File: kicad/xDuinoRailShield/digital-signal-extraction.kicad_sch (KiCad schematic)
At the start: 8 parts, among them U2 6N137, U3 EL817

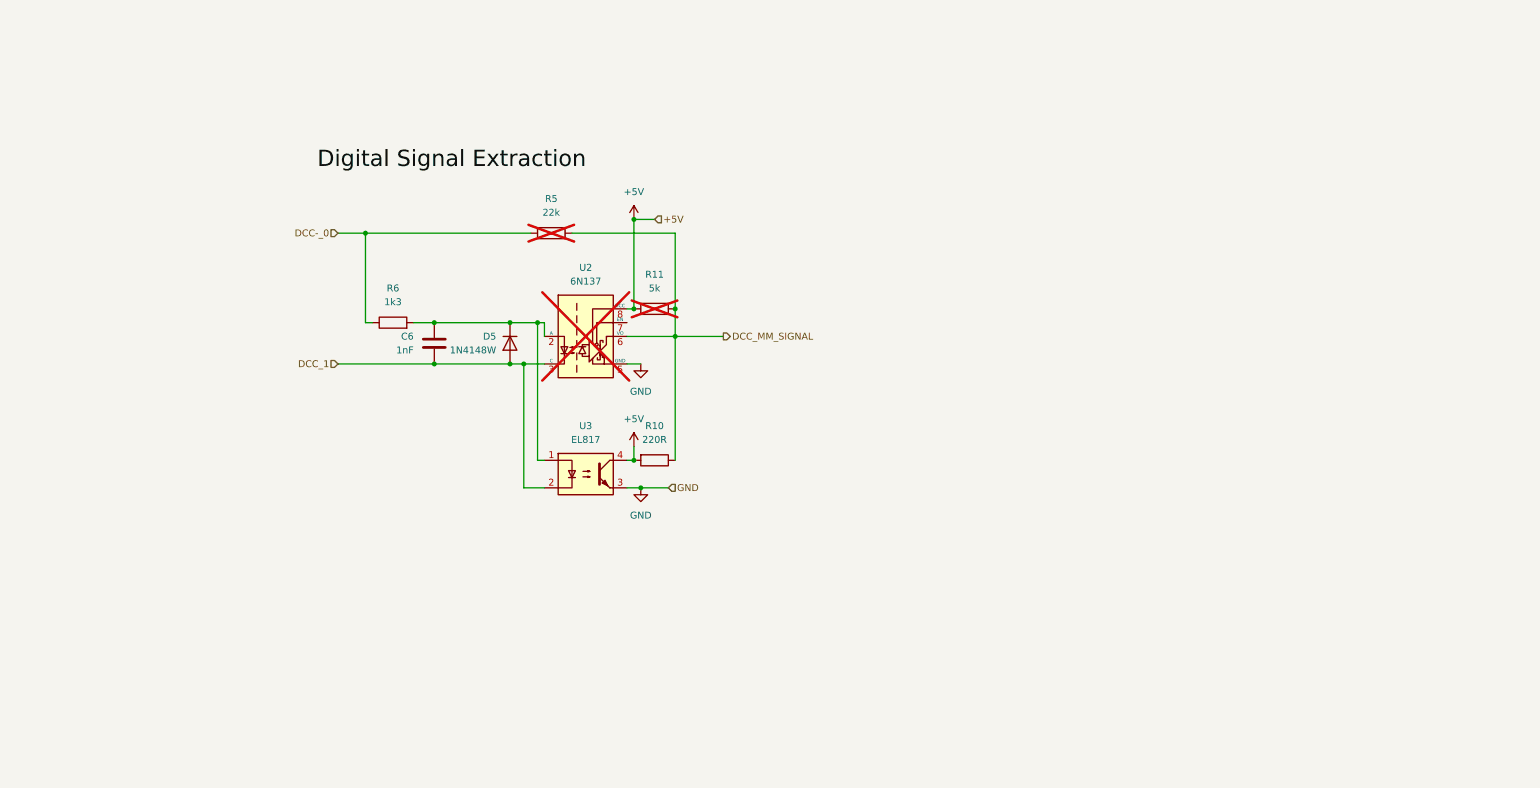
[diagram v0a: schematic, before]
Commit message: Add more extractor
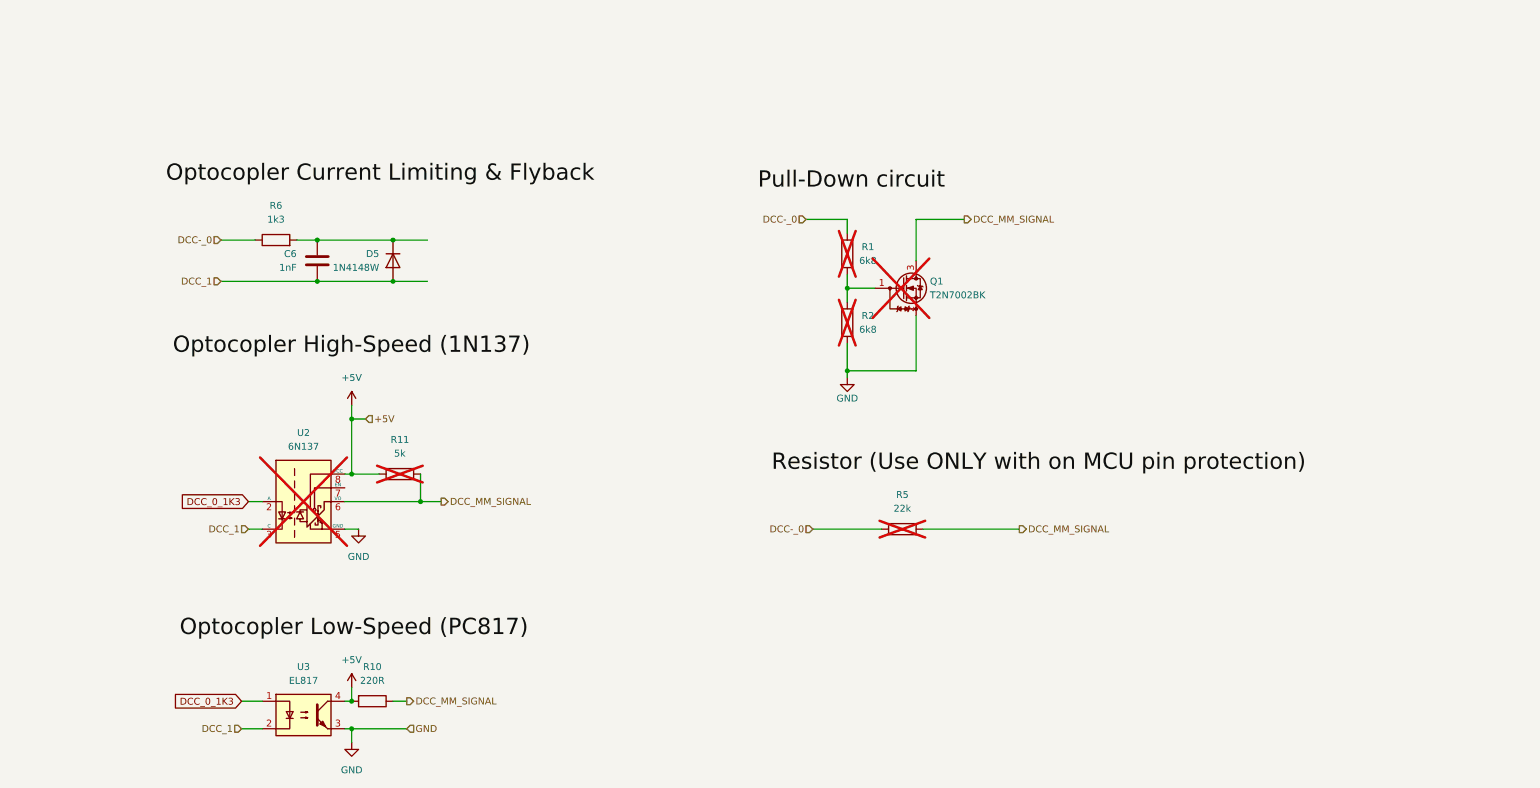
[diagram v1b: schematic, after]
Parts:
- added Q1: T2N7002BK, Package_TO_SOT_SMD:SOT-23, symbol RP2040-Decoder_Additional_Symbols:T2N7002BK
- added R1, R2: 6k8, RP2040-Decoder_Additional_Footprints:R_0603_1608Metric, symbol Device:R
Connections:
- net DCC_MM_SIGNAL: now also Q1.3 (D)
- net DCC­_0: now also R1.2
- net GND: now also Q1.2 (S), R2.1
- net at C6.1, D5.1 (K), R6.2: no longer U2.2 (A), U3.1
- new net: Q1.1 (G), R1.1, R2.2
- new net DCC_0_1K3: U2.2 (A), U3.1
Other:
- moved on the sheet: C6, D5, R6

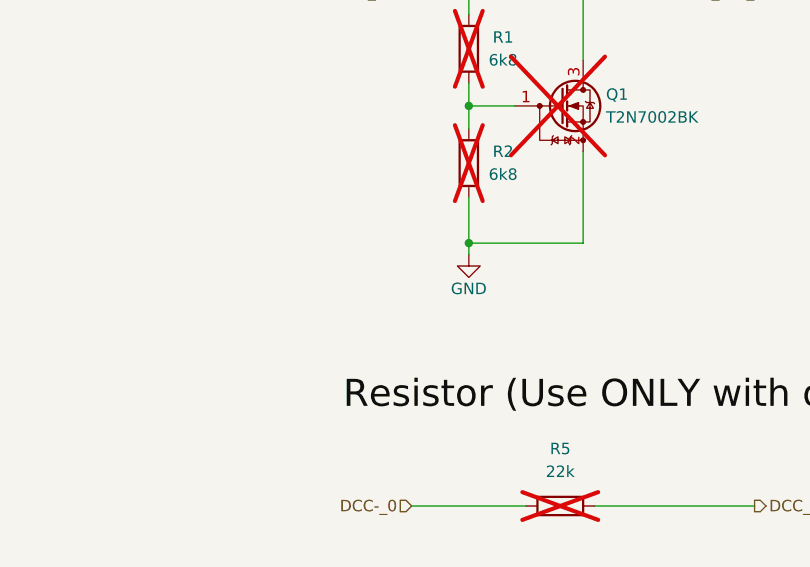
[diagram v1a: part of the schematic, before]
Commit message: More options, more Partnumbers
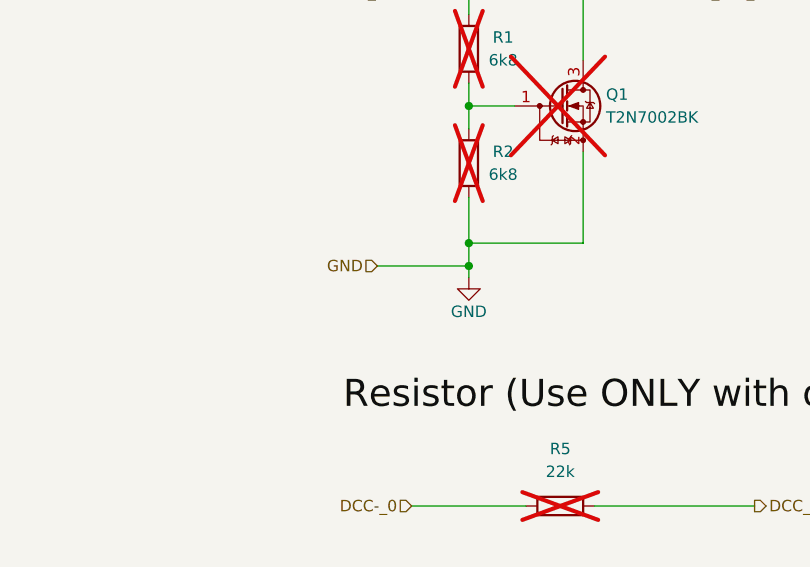
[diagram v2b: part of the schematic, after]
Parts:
- Q1: LCSC (none) -> C8545
- R1, R2: footprint RP2040-Decoder_Additional_Footprints:R_0603_1608Metric -> Resistor_SMD:R_0805_2012Metric_Pad1.20x1.40mm_HandSolder; LCSC (none) -> C17772
- R5: now left out of the parts list
- U2: LCSC (none) -> C16496; now left out of the parts list
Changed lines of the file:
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@@
   (junction (at 74.93 148.59) (diameter 0) (color 0 0 0 0)
   )
+  (junction (at 166.37 90.17) (diameter 0) (color 0 0 0 0)
+  )
   (junction (at 87.63 111.76) (diameter 0) (color 0 0 0 0)
   )
@@
     (stroke (width 0) (type default))
   )
+  (wire (pts (xy 156.21 90.17) (xy 166.37 90.17))
+    (stroke (width 0) (type default))
+  )
   (wire (pts (xy 179.07 77.47) (xy 179.07 87.63))
     (stroke (width 0) (type default))
@@
     (stroke (width 0) (type default))
   )
+  (wire (pts (xy 166.37 90.17) (xy 166.37 87.63))
+    (stroke (width 0) (type default))
+  )
   (wire (pts (xy 166.37 72.39) (xy 171.45 72.39))
     (stroke (width 0) (type default))
@@
     (stroke (width 0) (type default))
   )
-  (wire (pts (xy 166.37 88.9) (xy 166.37 87.63))
+  (wire (pts (xy 166.37 91.44) (xy 166.37 90.17))
     (stroke (width 0) (type default))
   )
@@
     (effects (font (size 1.27 1.27)) (justify left))
   )
+  (hierarchical_label "GND" (shape input) (at 156.21 90.17 180) (fields_autoplaced)
+    (effects (font (size 1.27 1.27)) (justify right))
+  )
   (hierarchical_label "DCC_1" (shape input) (at 54.61 153.67 180) (fields_autoplaced)
     (effects (font (size 1.27 1.27)) (justify right))
@@
   )
   (symbol (lib_id "Device:R") (at 166.37 66.04 180) (unit 1)
-    (in_bom no) (on_board no) (dnp yes)
+    (in_bom no) (on_board yes) (dnp yes)
     (property "Reference" "R1" (at 170.18 64.77 0)
       (effects (font (size 1.27 1.27)))
@@
       (effects (font (size 1.27 1.27)))
     )
-    (property "Footprint" "RP2040-Decoder_Additional_Footprints:R_0603_1608Metric" (at 168.148 66.04 90)
+    (property "Footprint" "Resistor_SMD:R_0805_2012Metric_Pad1.20x1.40mm_HandSolder" (at 168.148 66.04 90)
       (effects (font (size 1.27 1.27)) hide)
     )
     (property "Datasheet" "~" (at 166.37 66.04 0)
+      (effects (font (size 1.27 1.27)) hide)
+    )
+    (property "LCSC" "C17772" (at 166.37 66.04 0)
       (effects (font (size 1.27 1.27)) hide)
     )
@@
       (project "xDuinoRailShield"
         (path "/e63e39d7-6ac0-4ffd-8aa3-1841a4541b55/b84a333b-f29e-43df-b84d-edef752a64aa"
-          (reference "R11") (unit 1)
+          (reference "R304") (unit 1)
         )
       )
@@
         )
         (path "/e63e39d7-6ac0-4ffd-8aa3-1841a4541b55/b84a333b-f29e-43df-b84d-edef752a64aa"
-          (reference "#PWR06") (unit 1)
+          (reference "#PWR0303") (unit 1)
         )
       )
@@
   )
   (symbol (lib_id "RP2040-Decoder_Additional_Symbols:T2N7002BK") (at 176.53 72.39 0) (unit 1)
-    (in_bom no) (on_board no) (dnp yes)
+    (in_bom no) (on_board yes) (dnp yes)
     (property "Reference" "Q1" (at 181.61 71.12 0)
       (effects (font (size 1.27 1.27)) (justify left))
@@
     )
     (property "Datasheet" "https://datasheet.lcsc.com/lcsc/1810271831_TOSHIBA-T2N7002BK-LM_C146372.pdf" (at 190.5 83.82 0)
+      (effects (font (size 1.27 1.27)) hide)
+    )
+    (property "LCSC" "C8545" (at 176.53 72.39 0)
       (effects (font (size 1.27 1.27)) hide)
     )
@@
       (project "xDuinoRailShield"
         (path "/e63e39d7-6ac0-4ffd-8aa3-1841a4541b55/b84a333b-f29e-43df-b84d-edef752a64aa"
-          (reference "Q5") (unit 1)
+          (reference "Q301") (unit 1)
         )
       )
@@
         )
         (path "/e63e39d7-6ac0-4ffd-8aa3-1841a4541b55/b84a333b-f29e-43df-b84d-edef752a64aa"
-          (reference "D4") (unit 1)
+          (reference "D301") (unit 1)
         )
       )
@@
         )
         (path "/e63e39d7-6ac0-4ffd-8aa3-1841a4541b55/b84a333b-f29e-43df-b84d-edef752a64aa"
-          (reference "#PWR02") (unit 1)
+          (reference "#PWR0301") (unit 1)
         )
       )
@@
         )
         (path "/e63e39d7-6ac0-4ffd-8aa3-1841a4541b55/b84a333b-f29e-43df-b84d-edef752a64aa"
-          (reference "R5") (unit 1)
+          (reference "R303") (unit 1)
         )
       )
@@
         )
         (path "/e63e39d7-6ac0-4ffd-8aa3-1841a4541b55/b84a333b-f29e-43df-b84d-edef752a64aa"
-          (reference "#PWR05") (unit 1)
+          (reference "#PWR0304") (unit 1)
         )
       )
@@
         )
         (path "/e63e39d7-6ac0-4ffd-8aa3-1841a4541b55/b84a333b-f29e-43df-b84d-edef752a64aa"
-          (reference "#PWR04") (unit 1)
-        )
-      )
-    )
-  )
-  (symbol (lib_id "power:GND") (at 166.37 88.9 0) (mirror y) (unit 1)
+          (reference "#PWR0302") (unit 1)
+        )
+      )
+    )
+  )
+  (symbol (lib_id "power:GND") (at 166.37 91.44 0) (mirror y) (unit 1)
     (in_bom yes) (on_board yes) (dnp no)
-    (property "Reference" "#PWR08" (at 166.37 95.25 0)
-      (effects (font (size 1.27 1.27)) hide)
-    )
-    (property "Value" "GND" (at 166.37 92.71 0)
-      (effects (font (size 1.27 1.27)))
-    )
-    (property "Footprint" "" (at 166.37 88.9 0)
-      (effects (font (size 1.27 1.27)) hide)
-    )
-    (property "Datasheet" "" (at 166.37 88.9 0)
+    (property "Reference" "#PWR08" (at 166.37 97.79 0)
+      (effects (font (size 1.27 1.27)) hide)
+    )
+    (property "Value" "GND" (at 166.37 95.25 0)
+      (effects (font (size 1.27 1.27)))
+    )
+    (property "Footprint" "" (at 166.37 91.44 0)
+      (effects (font (size 1.27 1.27)) hide)
+    )
+    (property "Datasheet" "" (at 166.37 91.44 0)
       (effects (font (size 1.27 1.27)) hide)
     )
@@
       (project "xDuinoRailShield"
         (path "/e63e39d7-6ac0-4ffd-8aa3-1841a4541b55/b84a333b-f29e-43df-b84d-edef752a64aa"
-          (reference "#PWR018") (unit 1)
+          (reference "#PWR0305") (unit 1)
         )
       )
@@
         )
         (path "/e63e39d7-6ac0-4ffd-8aa3-1841a4541b55/b84a333b-f29e-43df-b84d-edef752a64aa"
-          (reference "U3") (unit 1)
+          (reference "U302") (unit 1)
         )
       )
@@
         )
         (path "/e63e39d7-6ac0-4ffd-8aa3-1841a4541b55/b84a333b-f29e-43df-b84d-edef752a64aa"
-          (reference "R6") (unit 1)
+          (reference "R302") (unit 1)
         )
       )
@@
         )
         (path "/e63e39d7-6ac0-4ffd-8aa3-1841a4541b55/b84a333b-f29e-43df-b84d-edef752a64aa"
-          (reference "C1") (unit 1)
+          (reference "C301") (unit 1)
         )
       )
@@
   )
   (symbol (lib_id "Device:R") (at 166.37 78.74 180) (unit 1)
-    (in_bom no) (on_board no) (dnp yes)
+    (in_bom no) (on_board yes) (dnp yes)
     (property "Reference" "R2" (at 170.18 77.47 0)
       (effects (font (size 1.27 1.27)))
@@
       (effects (font (size 1.27 1.27)))
     )
-    (property "Footprint" "RP2040-Decoder_Additional_Footprints:R_0603_1608Metric" (at 168.148 78.74 90)
+    (property "Footprint" "Resistor_SMD:R_0805_2012Metric_Pad1.20x1.40mm_HandSolder" (at 168.148 78.74 90)
       (effects (font (size 1.27 1.27)) hide)
     )
     (property "Datasheet" "~" (at 166.37 78.74 0)
+      (effects (font (size 1.27 1.27)) hide)
+    )
+    (property "LCSC" "C17772" (at 166.37 78.74 0)
       (effects (font (size 1.27 1.27)) hide)
     )
@@
       (project "xDuinoRailShield"
         (path "/e63e39d7-6ac0-4ffd-8aa3-1841a4541b55/b84a333b-f29e-43df-b84d-edef752a64aa"
-          (reference "R14") (unit 1)
+          (reference "R305") (unit 1)
         )
       )
@@
   )
   (symbol (lib_id "Device:R") (at 176.53 116.84 90) (unit 1)
-    (in_bom yes) (on_board yes) (dnp yes) (fields_autoplaced)
+    (in_bom no) (on_board yes) (dnp yes) (fields_autoplaced)
     (property "Reference" "R5" (at 176.53 110.49 90)
       (effects (font (size 1.27 1.27)))
@@
         )
         (path "/e63e39d7-6ac0-4ffd-8aa3-1841a4541b55/b84a333b-f29e-43df-b84d-edef752a64aa"
-          (reference "R4") (unit 1)
+          (reference "R306") (unit 1)
         )
       )
@@
         )
         (path "/e63e39d7-6ac0-4ffd-8aa3-1841a4541b55/b84a333b-f29e-43df-b84d-edef752a64aa"
-          (reference "R3") (unit 1)
+          (reference "R301") (unit 1)
         )
       )
@@
   )
   (symbol (lib_id "Isolator:6N137") (at 66.04 111.76 0) (unit 1)
-    (in_bom yes) (on_board yes) (dnp yes) (fields_autoplaced)
+    (in_bom no) (on_board yes) (dnp yes) (fields_autoplaced)
     (property "Reference" "U2" (at 66.04 99.06 0)
       (effects (font (size 1.27 1.27)))
@@
       (effects (font (size 1.27 1.27)) hide)
     )
-    (property "LCSC" "" (at 66.04 111.76 0)
+    (property "LCSC" "C16496" (at 66.04 111.76 0)
       (effects (font (size 1.27 1.27)) hide)
     )
@@
         )
         (path "/e63e39d7-6ac0-4ffd-8aa3-1841a4541b55/b84a333b-f29e-43df-b84d-edef752a64aa"
-          (reference "U2") (unit 1)
-        )
-      )
+          (reference "U301") (unit 1)
+        )
+      )

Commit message: Another iteration on the layout
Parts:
- U302: renamed from U3; footprint Package_DIP:DIP-4_W7.62mm_SMDSocket_SmallPads -> Package_DIP:DIP-4_W8.89mm_SMDSocket_LongPads
- renumbered C6 to C301, D5 to D301, R6 to R301, R10 to R302, R11 to R303, U2 to U301
